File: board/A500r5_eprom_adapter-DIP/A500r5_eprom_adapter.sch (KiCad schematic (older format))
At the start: 11 parts, among them J2 A18 Selector, J3 A19 Selector, U1 27C400-A500, U2 27C080-L, U3 27C080-L

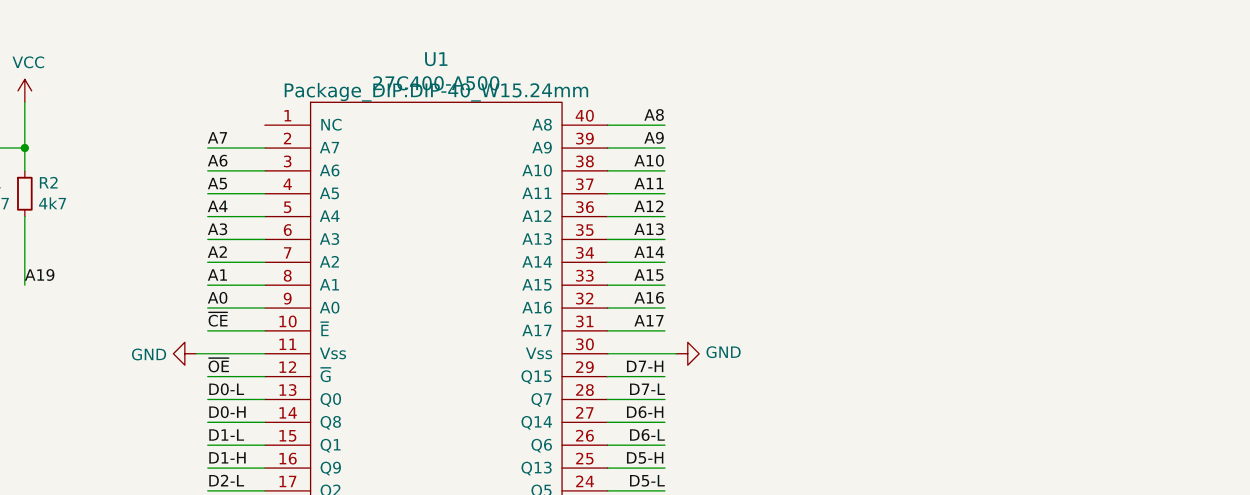
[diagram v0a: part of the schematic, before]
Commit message: Add A17 pin selector
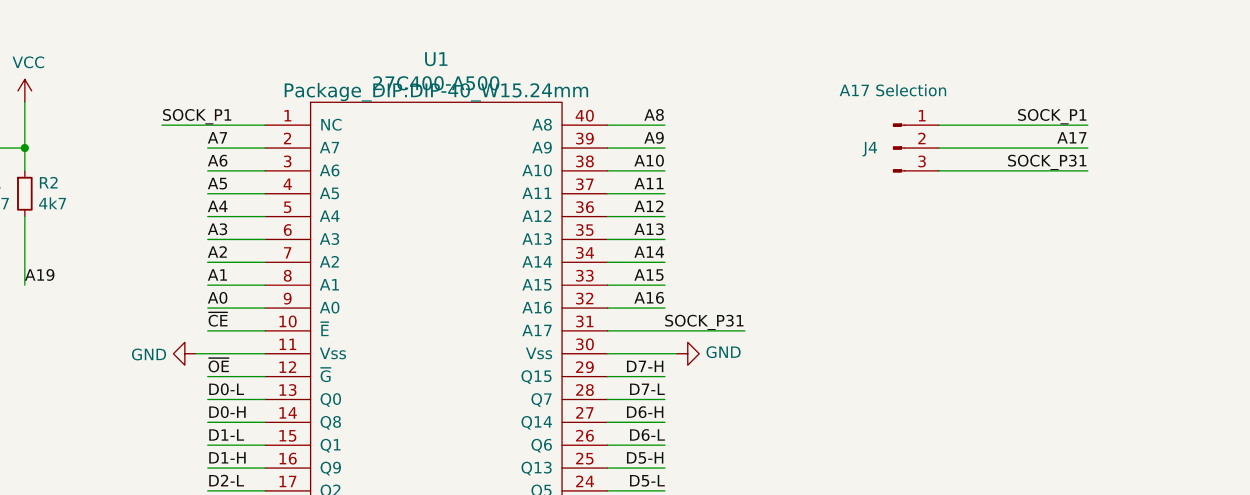
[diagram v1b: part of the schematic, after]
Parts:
- added J4: A17 Selection, Connector_PinHeader_2.54mm:PinHeader_1x03_P2.54mm_Vertical, symbol Connector:Conn_01x03_Male
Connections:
- net A17: now also J4.2 (Pin_2); no longer U1.31 (A17)
- net SOCK_P1: now reaches U1.1 (NC)
- net SOCK_P1: now also J4.1 (Pin_1)
- new net SOCK_P31: J4.3 (Pin_3), U1.31 (A17)
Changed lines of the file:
@@
 	5200 2000 4950 2000
-Wire Wire Line
-	5200 2100 4950 2100
 Wire Wire Line
 	3450 2100 3200 2100
@@
 Text Label 5200 2000 2    50   ~ 0
 A16
-Text Label 5200 2100 2    50   ~ 0
-A17
 Text Label 5200 3000 2    50   ~ 0
 D4-L
@@
 	2400 1100 2400 1300
 Connection ~ 2400 1300
+$Comp
+L Connector:Conn_01x03_Male J4
+U 1 1 5F417023
+P 6200 1300
+F 0 "J4" H 6100 1300 50  0000 C CNN
+F 1 "A17 Selection" H 6200 1550 50  0000 C CNN
+F 2 "Connector_PinHeader_2.54mm:PinHeader_1x03_P2.54mm_Vertical" H 6200 1300 50  0001 C CNN
+F 3 "~" H 6200 1300 50  0001 C CNN
+	1    6200 1300
+	1    0    0    -1
+$EndComp
+Wire Wire Line
+	6400 1200 7050 1200
+Wire Wire Line
+	6400 1300 7050 1300
+Wire Wire Line
+	6400 1400 7050 1400
+Text Label 7050 1300 2    50   ~ 0
+A17
+Text Label 7050 1200 2    50   ~ 0
+SOCK_P1
+Text Label 7050 1400 2    50   ~ 0
+SOCK_P31
+Wire Wire Line
+	4950 2100 5550 2100
+Wire Wire Line
+	3450 1200 3000 1200
+Text Label 5550 2100 2    50   ~ 0
+SOCK_P31
+Text Label 3000 1200 0    50   ~ 0
+SOCK_P1
 $EndSCHEMATC
